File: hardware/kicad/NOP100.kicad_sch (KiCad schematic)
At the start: 45 parts, among them CON1 CLICK MODULE 0, CON2 CLICK MODULE 1, J1 CAN, Q1 BSS138, Q2 BSS138, SW1 BUS, SW2 SW_Push, U1 MURATA_MEJ2*, U2 MCP2551-I-P, U3 Teensy_4.0, U4 74HC165, U6 NCS1S1203SC

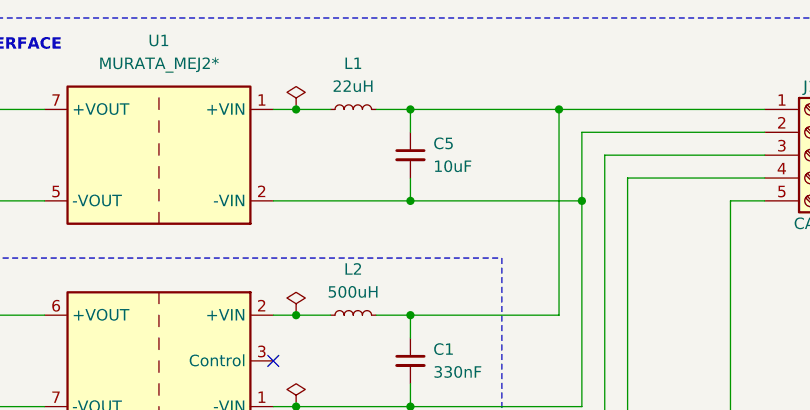
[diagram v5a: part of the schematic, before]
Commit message: Update GPIO assignments.
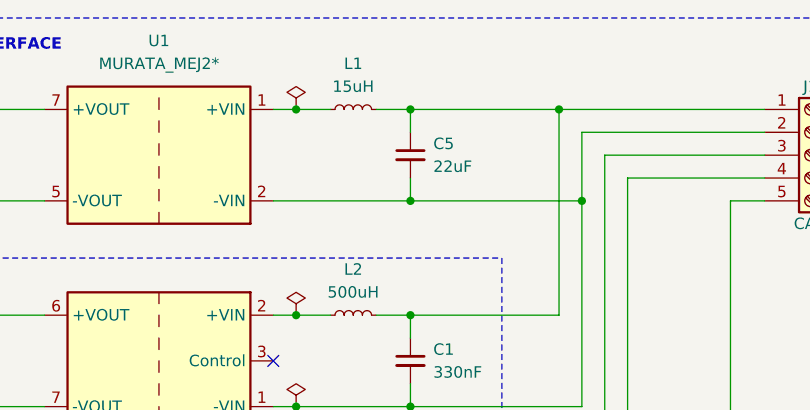
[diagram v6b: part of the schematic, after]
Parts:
- C5: value 10uF -> 22uF
- L1: value 22uH -> 15uH; footprint Inductor_SMD:L_Bourns_SRU5016_5.2x5.2mm -> Inductor_SMD:L_Bourns_SRN6045TA
- L2: footprint Inductor_SMD:L_Bourns_SRU5016_5.2x5.2mm -> Inductor_SMD:L_Bourns_SRN6045TA
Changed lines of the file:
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@@
       (effects (font (size 1.27 1.27)) (justify left))
     )
-    (property "Value" "10uF" (at 90.17 30.4863 0)
+    (property "Value" "22uF" (at 90.17 30.4863 0)
       (effects (font (size 1.27 1.27)) (justify left))
     )
@@
       (effects (font (size 1.27 1.27)))
     )
-    (property "Value" "22uH" (at 81.28 21.59 90)
-      (effects (font (size 1.27 1.27)))
-    )
-    (property "Footprint" "Inductor_SMD:L_Bourns_SRU5016_5.2x5.2mm" (at 81.28 24.13 0)
+    (property "Value" "15uH" (at 81.28 21.59 90)
+      (effects (font (size 1.27 1.27)))
+    )
+    (property "Footprint" "Inductor_SMD:L_Bourns_SRN6045TA" (at 81.28 24.13 0)
       (effects (font (size 1.27 1.27)) hide)
     )
@@
       (effects (font (size 1.27 1.27)))
     )
-    (property "Footprint" "Inductor_SMD:L_Bourns_SRU5016_5.2x5.2mm" (at 81.28 46.99 0)
-      (effects (font (size 1.27 1.27)) hide)
-    )
+    (property "Footprint" "Inductor_SMD:L_Bourns_SRN6045TA" (at 81.28 46.99 0)
+      (effects (font (size 1.27 1.27)) hide)
+    )
